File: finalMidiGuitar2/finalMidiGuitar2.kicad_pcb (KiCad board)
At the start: 2 copper layers, 67.3 x 30.2 mm, 41 parts, among them J1 PinHeader_01x06_P2.54mm_Verti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, J3 NeoPixel, J4 Oled Display, M1 Module_XIAO_Generic_SocketSMD, SW1 BTN, U1 SN74LVC1T45DBVR

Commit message: Remove lock files for KiCad PCB and schematic
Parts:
- added ?: , , F.Cu at (124.6, 138.0)
- added ? (x4): , , F.Cu at (124.6, 139.2)
- added ? (x2): , , F.Cu at (124.6, 138.6)
- added C4: 0.1uf, PCM_fab:C_1206, F.Cu at (141.2, 132.2)
- added C5: 0.1uf, PCM_fab:C_1206, F.Cu at (131.9, 126.4)
- added D1: Diode_Schottky_MiniSMA, PCM_fab:Diode_Schottky_MiniSMA, F.Cu at (148.5, 131.3)
- added R2: 10 kΩ, PCM_fab:R_1206, F.Cu at (135.8, 122.3)
- added R3: 10 kΩ, PCM_fab:R_1206, F.Cu at (127.9, 132.6)
- added R4: 10 kΩ, PCM_fab:R_1206, F.Cu at (131.9, 132.9)
- added R5: 0, PCM_fab:R_1206, F.Cu at (128.1, 126.3)
- added R7: 0, PCM_fab:R_1206, F.Cu at (131.7, 121.2)
- added R8: 0, PCM_fab:R_1206, F.Cu at (141.4, 135.0)
- added REF**: MountingHole_M2, PCM_fab:MountingHole_M2, F.Cu at (124.6, 138.0)
- U1: value SN74LVC1T45DBVR -> LevelShifter; footprint footprints:DBV0006A_N -> PCM_fab:LevelShifter_Texas_TXB0104DR_SOIC-14
- moved J3 15.5 mm to (150.1, 121.7), turned to 180 degrees
- moved R1 10.6 mm to (145.9, 120.4)
- moved C3 2.09 mm to (148.4, 124.7)
- moved C2 1.89 mm to (148.1, 127.7)
- moved SW1 1.50 mm to (158.4, 117.4)
- moved ? 0.18 mm to (124.6, 116.8) (x2)
- moved ? 0.18 mm to (124.6, 116.2)
- moved REF** 0.18 mm to (124.6, 115.6)
- moved C1 0.16 mm to (135.8, 127.2)
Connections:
- C3 pad 2: PWR_5V -> 4V5_NEO
- J3 pad 2: PWR_5V -> 4V5_NEO
- R1 pad 1: Net-(U1-B) -> Net-(U1-B1)
- U1 pad 2: PWR_GND -> Net-(M1-D10)
- U1 pad 3: Net-(M1-D10) -> Net-(U1-A2)
- U1 pad 4: Net-(U1-B) -> Net-(U1-A3)
- U1 pad 5: PWR_3V3 -> Net-(U1-A4)
- U1 pad 6: PWR_5V -> unconnected-(U1-NC-Pad6)
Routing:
- net 4V5_NEO: track 0.00 -> 46.6 mm
- net PWR_GND: track 101.5 -> 133.7 mm
- net PWR_5V: track 91.0 -> 70.5 mm
- net PWR_3V3: track 140.0 -> 158.8 mm
- net Net-(J3-Pin_1): track 20.3 -> 3.16 mm
- net Net-(U1-A3): track 0.00 -> 14.2 mm
- net Net-(U1-A4): track 0.00 -> 9.38 mm
- net Net-(U1-B1): track 0.00 -> 5.67 mm
- net Net-(U1-B): track 3.83 -> 0.00 mm
- net Net-(U1-A2): track 0.00 -> 3.26 mm
- net Net-(M1-D10): track 64.0 -> 65.6 mm
- net Net-(M1-D2): track 37.0 -> 35.6 mm
- net SCL: track 73.7 -> 74.6 mm

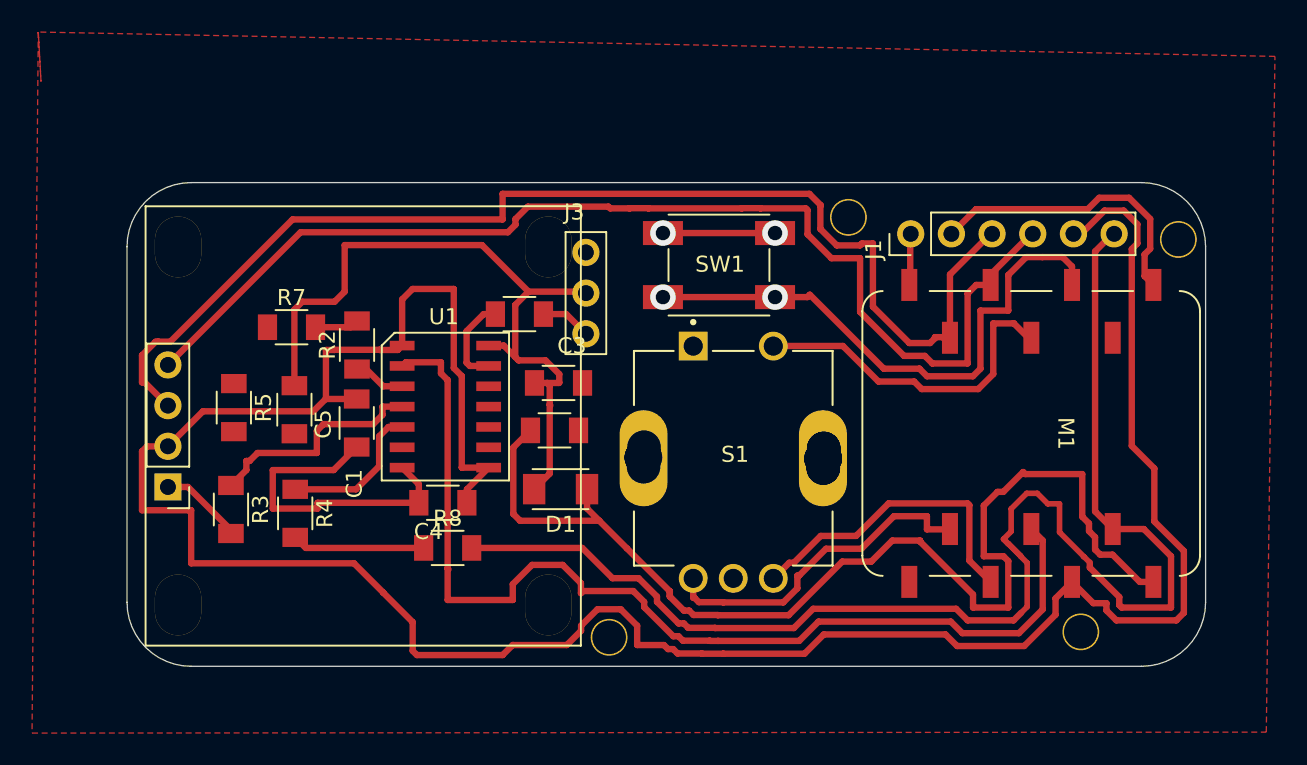
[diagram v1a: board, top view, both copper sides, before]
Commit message: Add new CAD and backup files for Midi Guitar project
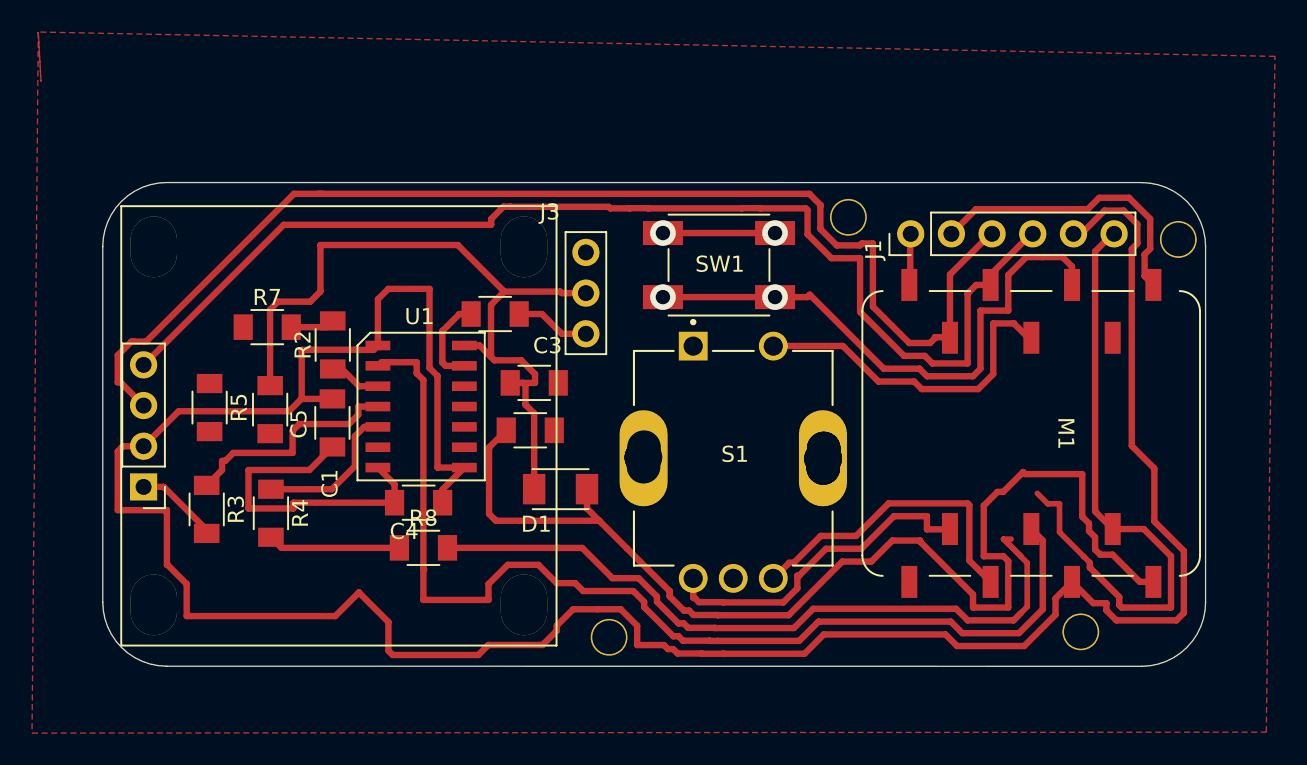
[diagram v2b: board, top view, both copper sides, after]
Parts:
- moved J4 1.52 mm to (122.5, 127.4)
- moved ? 1.51 mm to (123.1, 138.0)
- moved ? 1.51 mm to (146.0, 138.5)
- moved ? 1.51 mm to (146.0, 139.1) (x2)
- moved ? 1.51 mm to (123.1, 139.2) (x2)
- moved ? 1.51 mm to (146.1, 116.2) (x2)
- moved ? 1.51 mm to (123.1, 116.8) (x2)
- moved ? 1.51 mm to (146.0, 116.5)
- moved ? 1.51 mm to (123.1, 116.2)
- moved ? 1.51 mm to (123.1, 138.6) (x2)
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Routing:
- net PWR_3V3: track 158.8 -> 162.8 mm
- net PWR_GND: track 133.7 -> 131.6 mm
- net PWR_5V: track 70.5 -> 72.2 mm
- net Net-(J3-Pin_1): track 3.16 -> 4.68 mm
- net SDA: track 71.8 -> 73.3 mm
- net Net-(M1-D10): track 65.6 -> 66.6 mm
- net SCL: track 74.6 -> 75.4 mm
- net 4V5_NEO: track 46.6 -> 47.4 mm
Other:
- board size 67.3 x 30.2 mm -> 68.9 x 30.2 mm
